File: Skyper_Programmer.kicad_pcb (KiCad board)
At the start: 2 copper layers, 73 x 48 mm, 21 parts, among them IC1 LM7805_TO220, IC2 MAX232, IC3 LP2950-3.0_TO92, K1 D-SUB9, K2 1x2, K3 1x4, T1 BC547, T2 BC547

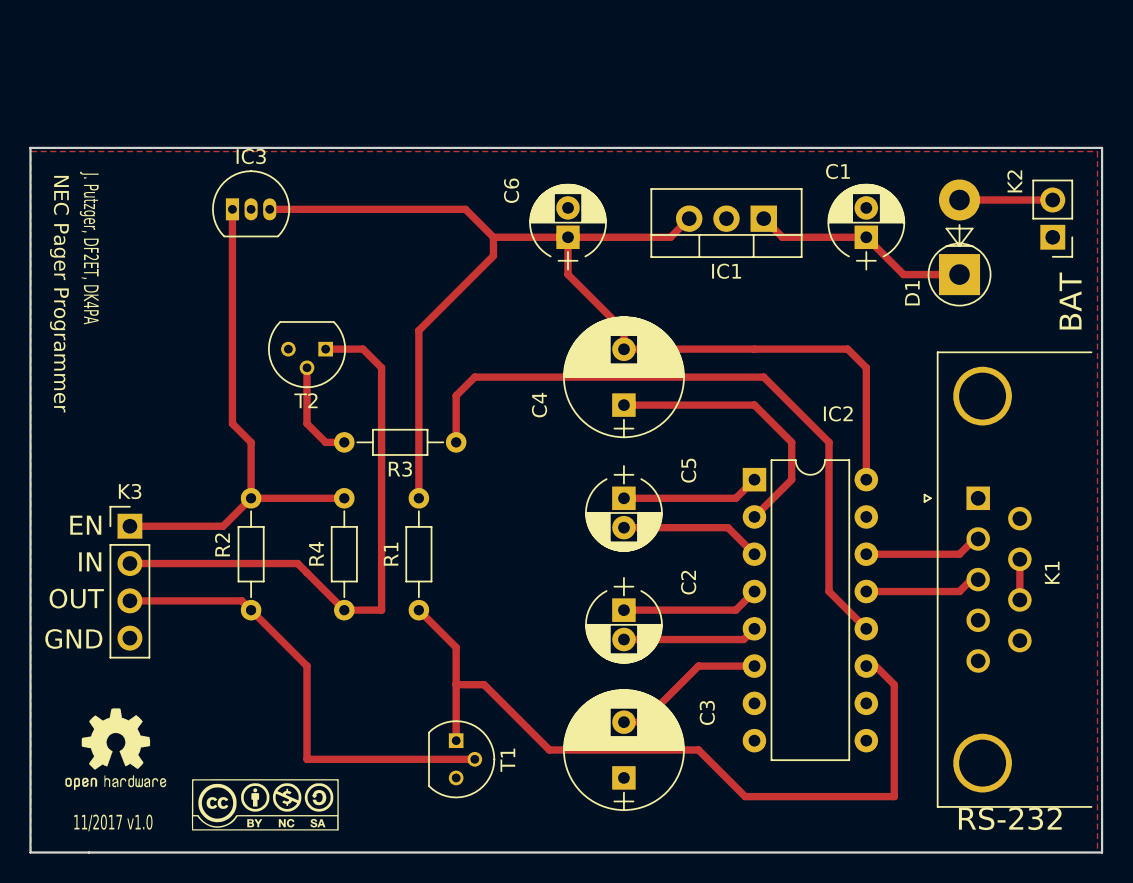
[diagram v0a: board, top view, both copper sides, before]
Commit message: Change parts to SMD
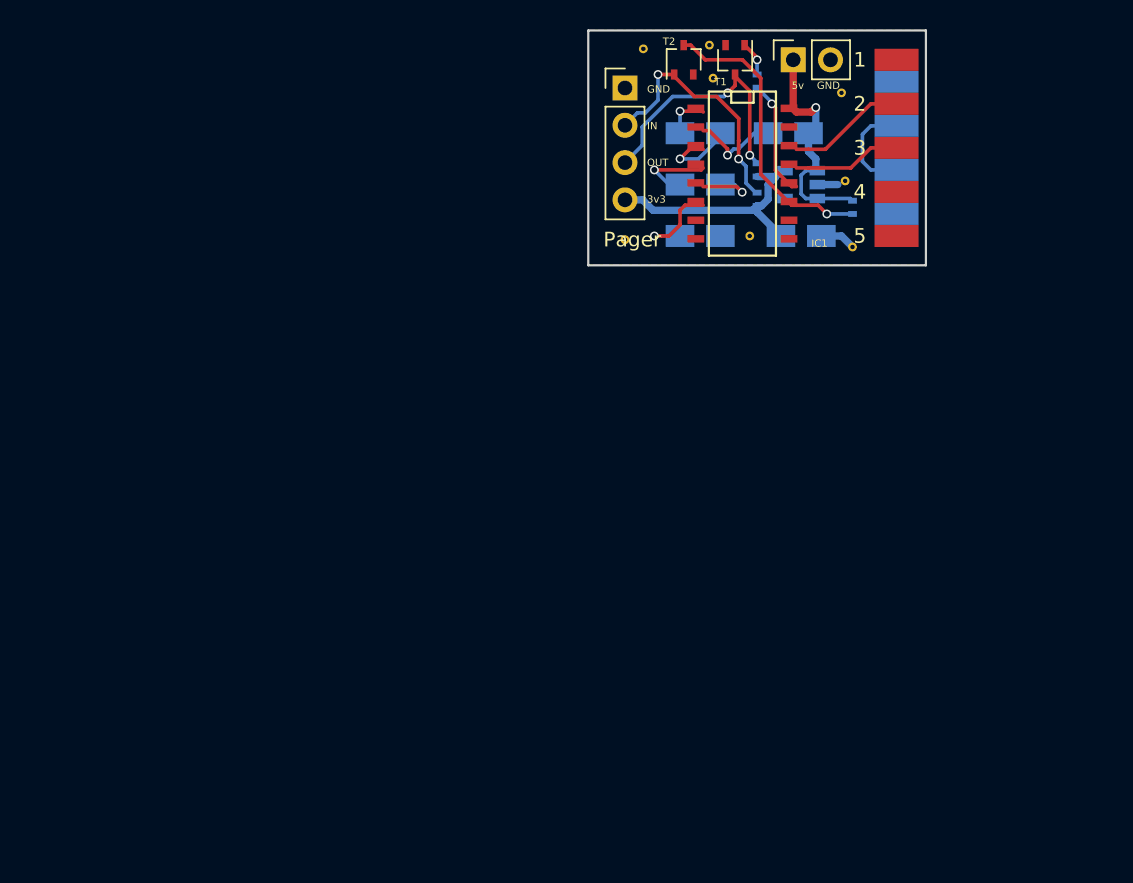
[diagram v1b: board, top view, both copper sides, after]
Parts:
- removed C6: 10µF, Capacitors_THT:CP_Radial_D5.0mm_P2.00mm
- removed D1: 1N4004, Diodes_THT:D_5W_P5.08mm_Vertical_AnodeUp
- removed G***: LOGO, OPENHARDWARE:OSHWLOGO0.3IN
- removed G***: LOGO, CC Logos:Logo_silk_CC-BY-NC-SA_10x3.6mm
- removed IC2: MAX232, Housings_DIP:DIP-16_W7.62mm
- removed IC3: LP2950-3.0_TO92, TO_SOT_Packages_THT:TO-92_Inline_Narrow_Oval
- removed K1: D-SUB9, Connectors_DSub:DSUB-9_Female_Horizontal_Pitch2.77x2.84mm_EdgePinOffset4.94mm_Housed_MountingHolesOffset7.48mm
- removed K2: 1x2, Pin_Headers:Pin_Header_Straight_1x02_Pitch2.54mm
- removed K3: 1x4, Pin_Headers:Pin_Header_Straight_1x04_Pitch2.54mm
- added J1: Pager, Connector_PinHeader_2.54mm:PinHeader_1x04_P2.54mm_Vertical, F.Cu at (138.5, 74.9)
- added J10: Pin9, SubD_Connector:SubD Pad, B.Cu at (157.0, 83.5)
- added J11: Pin5, SubD_Connector:SubD Pad, F.Cu at (157.0, 85.0)
- added J2: USB PWR, Connector_PinSocket_2.54mm:PinSocket_1x02_P2.54mm_Vertical, F.Cu at (150.0, 73.0)
- added J3: Pin1, SubD_Connector:SubD Pad, F.Cu at (157.0, 73.0)
- added J4: Pin6, SubD_Connector:SubD Pad, B.Cu at (157.0, 74.5)
- added J5: Pin2, SubD_Connector:SubD Pad, F.Cu at (157.0, 76.0)
- added J6: Pin7, SubD_Connector:SubD Pad, B.Cu at (157.0, 77.5)
- added J7: Pin3, SubD_Connector:SubD Pad, F.Cu at (157.0, 79.0)
- added J8: Pin8, SubD_Connector:SubD Pad, B.Cu at (157.0, 80.5)
- added J9: Pin4, SubD_Connector:SubD Pad, F.Cu at (157.0, 82.0)
- added REF**: VIA-0.6mm, SubD_Connector:VIA-0.6mm, F.Cu at (144.2, 72.0)
- added REF**: VIA-0.6mm, SubD_Connector:VIA-0.6mm, F.Cu at (144.5, 74.2)
- added REF**: VIA-0.6mm, SubD_Connector:VIA-0.6mm, F.Cu at (154.0, 85.8)
- added REF**: VIA-0.6mm, SubD_Connector:VIA-0.6mm, F.Cu at (138.5, 85.2)
- added REF**: VIA-0.6mm, SubD_Connector:VIA-0.6mm, F.Cu at (139.8, 72.2)
- added REF**: VIA-0.6mm, SubD_Connector:VIA-0.6mm, F.Cu at (153.2, 75.2)
- added REF**: VIA-0.6mm, SubD_Connector:VIA-0.6mm, F.Cu at (153.5, 81.2)
- added REF**: VIA-0.6mm, SubD_Connector:VIA-0.6mm, F.Cu at (147.0, 85.0)
- added U1: TC1055, Package_TO_SOT_SMD:SOT-23-5, B.Cu at (150.5, 81.5)
- C1, C2, C5: footprint Capacitors_THT:CP_Radial_D5.0mm_P2.00mm -> Capacitors_Tantalum_SMD:CP_Tantalum_Case-A_EIA-3216-18_Reflow; moved to B.Cu
- C3, C4: footprint Capacitors_THT:CP_Radial_D8.0mm_P3.80mm -> Capacitors_Tantalum_SMD:CP_Tantalum_Case-A_EIA-3216-18_Reflow; moved to B.Cu
- IC1: value LM7805_TO220 -> MAX232; footprint TO_SOT_Packages_THT:TO-220-3_Vertical -> SMD_Packages:SO-16-N
- R1, R2, R3, R4: footprint Resistors_THT:R_Axial_DIN0204_L3.6mm_D1.6mm_P7.62mm_Horizontal -> Resistors_SMD:R_0402; moved to B.Cu
- T1, T2: value BC547 -> BC847; footprint TO_SOT_Packages_THT:TO-92_Molded_Narrow -> TO_SOT_Packages_SMD:SOT-323_SC-70
- moved T1 50.1 mm to (146.0, 73.0)
- moved R2 44.4 mm to (147.5, 82.5), turned to 270 degrees
- moved R4 44.2 mm to (154.0, 83.0)
- moved C3 40.8 mm to (143.6, 81.5), turned to 0 degrees
- moved R1 37.8 mm to (147.5, 80.5), turned to 270 degrees
- moved C2 32.9 mm to (143.6, 78.0), turned to 0 degrees
- moved R3 32.0 mm to (147.5, 74.5), turned to 90 degrees
- moved T2 31.4 mm to (142.5, 73.0), turned to 90 degrees
- moved C5 27.3 mm to (149.6, 78.0), turned to 0 degrees
- moved C4 12.6 mm to (143.6, 85.0), turned to 180 degrees
- moved C1 4.44 mm to (150.5, 85.0), turned to 0 degrees
- moved IC1 3.40 mm to (146.5, 80.8), turned to 270 degrees
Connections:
- C1 pad 1: +BATT -> +3V0
- C3 pad 1: GND -> Net-(C3-Pad1)
- C4 pad 1: Net-(C4-Pad1) -> GND
- C4 pad 2: +5V -> Net-(C4-Pad2)
- C5 pad 2: Net-(C5-Pad2) -> +5V
- IC1 pad 1: +BATT -> Net-(C2-Pad1)
- IC1 pad 2: GND -> Net-(C5-Pad1)
- IC1 pad 3: +5V -> Net-(C2-Pad2)
- R1 pad 1: Net-(IC2-Pad11) -> Net-(J1-Pad3)
- R1 pad 2: +5V -> +3V0
- R2 pad 1: Net-(K3-Pad3) -> Net-(J1-Pad2)
- R3 pad 1: Net-(IC2-Pad12) -> Net-(IC1-Pad12)
- R4 pad 1: Net-(K3-Pad2) -> Net-(IC1-Pad11)
- R4 pad 2: +3V0 -> +5V
- T1 pad 1: Net-(IC2-Pad11) -> Net-(R3-Pad2)
- T1 pad 2: Net-(K3-Pad3) -> GND
- T1 pad 3: GND -> Net-(J1-Pad3)
- T2 pad 1: Net-(K3-Pad2) -> Net-(J1-Pad2)
- T2 pad 2: Net-(R3-Pad2) -> GND
- T2 pad 3: GND -> Net-(IC1-Pad11)
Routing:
- net +5V: track 83.6 -> 15.9 mm, vias 0 -> 1
- net Net-(IC2-Pad11): track 53.0 -> 0.00 mm
- net Net-(IC2-Pad12): track 44.7 -> 0.00 mm
- net Net-(K3-Pad2): track 39.3 -> 0.00 mm
- net Net-(K3-Pad3): track 31.7 -> 0.00 mm
- net Net-(IC1-Pad11): track 0.00 -> 20.1 mm, vias 0 -> 1
- net +3V0: track 35.6 -> 16.9 mm
- net Net-(C4-Pad1): track 18.6 -> 0.00 mm
- net Net-(J1-Pad3): track 0.00 -> 17.8 mm, vias 0 -> 2
- net Net-(J1-Pad2): track 0.00 -> 17.2 mm, vias 0 -> 2
- net +BATT: track 14.9 -> 0.00 mm
- net Net-(C5-Pad2): track 9.64 -> 0.00 mm
- net Net-(IC1-Pad14): track 0.00 -> 8.11 mm
- net Net-(IC2-Pad14): track 8.05 -> 0.00 mm
- net Net-(IC1-Pad12): track 0.00 -> 8.03 mm, vias 0 -> 1
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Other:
- board size 73 x 48 mm -> 23 x 16 mm
- board text added: "1"
- board text added: "2"
- board text added: "3"
- board text added: "3v3"
- board text added: "4"
- board text added: "5"
- board text added: "5v GND"
- board text added: "6"
- board text added: "7"
- board text added: "8"
- board text added: "9"
- board text added: "Pager"
- board text removed: "11/2017 v1.0"
- board text removed: "BAT"
- board text removed: "EN"
- board text removed: "J. Putzger, DF2ET, DK4PA"
- board text removed: "NEC Pager Programmer"
- board text removed: "RS-232"

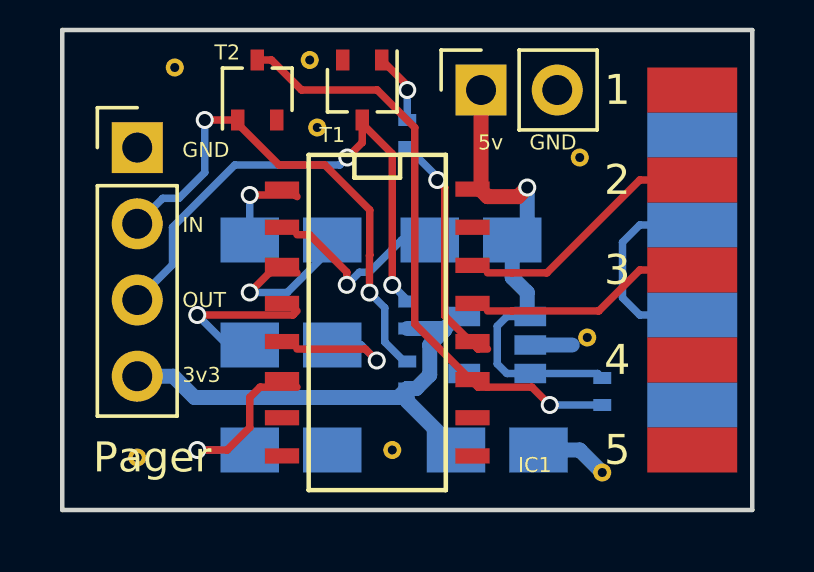
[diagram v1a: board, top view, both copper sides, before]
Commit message: Add some Text to PCB
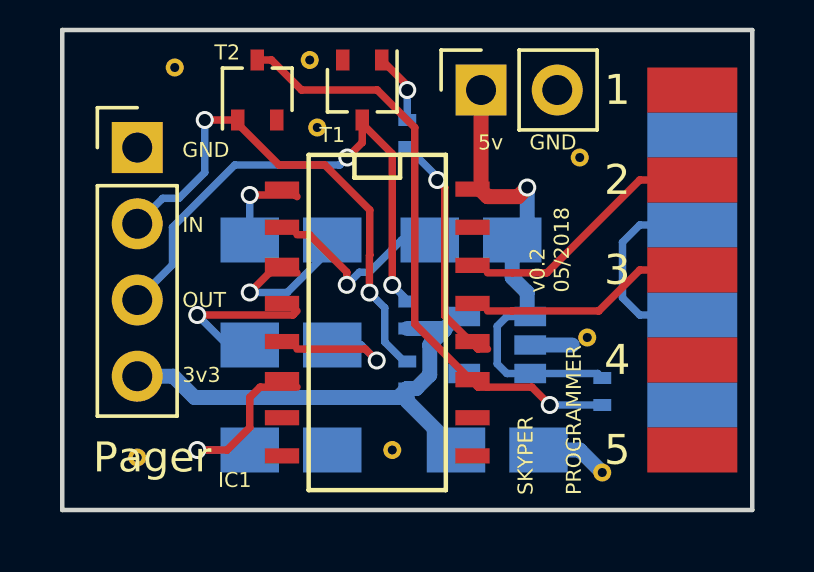
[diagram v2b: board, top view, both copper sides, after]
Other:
- board text added: "(C) DF2ET DK4PA CC-BY-SA-NC"
- board text added: "SKYPER PROGRAMMER"
- board text added: "v0.2 05/2018"
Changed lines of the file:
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@@
-(kicad_pcb (version 20171130) (host pcbnew 5.0.0-rc2-dev-unknown-8f6ae70~65~ubuntu18.04.1)
+(kicad_pcb (version 20171130) (host pcbnew 5.0.0-rc2-dev-unknown-538ab0e~65~ubuntu18.04.1)
   (general
     (thickness 1.6)
-    (drawings 21)
+    (drawings 24)
     (tracks 137)
     (zones 0)
@@
     (tags "CMS SOJ")
     (attr smd)
-    (fp_text reference IC1 (at 4.75 -5.25) (layer F.SilkS)
+    (fp_text reference IC1 (at 5.25 4.75) (layer F.SilkS)
       (effects (font (size 0.5 0.5) (thickness 0.125)))
     )
@@
       (rotate (xyz 0 0 0))
     )
+  )
+  (gr_text "(C) DF2ET DK4PA\nCC-BY-SA-NC" (at 146.75 73.25) (layer B.SilkS)
+    (effects (font (size 0.5 0.5) (thickness 0.125)) (justify left mirror))
+  )
+  (gr_text "v0.2\n05/2018" (at 152.25 79.75 90) (layer F.SilkS)
+    (effects (font (size 0.5 0.5) (thickness 0.125)) (justify left))
+  )
+  (gr_text "SKYPER\n\nPROGRAMMER" (at 152.25 86.5 90) (layer F.SilkS)
+    (effects (font (size 0.5 0.5) (thickness 0.125)) (justify left))
   )
   (gr_text Pager (at 139 85.25) (layer F.SilkS)
@@
       )
     )
+  )
+  (zone (net 0) (net_name "") (layer B.Cu) (hatch edge 0.508)
+    (connect_pads (clearance 0.508))
+    (min_thickness 0.254)
+    (keepout (tracks not_allowed) (vias not_allowed) (copperpour not_allowed))
+    (fill (arc_segments 16) (thermal_gap 0.508) (thermal_bridge_width 0.508))
+    (polygon
+      (pts
+        (xy 155 73.5) (xy 159 73.5) (xy 159 71.5) (xy 155 71.5)
+      )
+    )
+  )
+  (zone (net 0) (net_name "") (layer B.Cu) (hatch edge 0.508)
+    (connect_pads (clearance 0.508))
+    (min_thickness 0.254)
+    (keepout (tracks not_allowed) (vias not_allowed) (copperpour not_allowed))
+    (fill (arc_segments 16) (thermal_gap 0.508) (thermal_bridge_width 0.508))
+    (polygon
+      (pts
+        (xy 155 84.5) (xy 159 84.5) (xy 159 86.5) (xy 155 86.5)
+      )
+    )
